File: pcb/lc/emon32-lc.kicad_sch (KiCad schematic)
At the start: 38 parts, among them J3 Conn_02x05_Odd_Even, J4 RJ12, J5 Conn_Coaxial, J6 USB_C_Receptacle_USB2.0, J7 Conn_01x03_Male, J8 Conn_02x04_Odd_Even, J9 Conn_01x03_Male, SW1 SW_Push, U2 AT24CS01-STUM, U3 ATSAMD11D14A-M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

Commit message: * [PCB LC]
  - Change to MCP1501 reference
  - Some retouching of traces
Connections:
- net UART_DBG_RX: now also J7.1 (Pin_1); no longer J7.2 (Pin_2)
- net UART_DBG_TX: now also J7.2 (Pin_2); no longer J7.1 (Pin_1)
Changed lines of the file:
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@@
     (effects (font (size 1.27 1.27)) (justify right bottom))
   )
-  (label "UART_DBG_RX" (at 139.7 91.44 0)
+  (label "UART_DBG_RX" (at 139.7 88.9 0)
     (effects (font (size 1.27 1.27)) (justify left bottom))
   )
@@
     (effects (font (size 1.27 1.27)) (justify right bottom))
   )
-  (label "UART_DBG_TX" (at 139.7 88.9 0)
+  (label "UART_DBG_TX" (at 139.7 91.44 0)
     (effects (font (size 1.27 1.27)) (justify left bottom))
   )
@@
       (reference "SW1") (unit 1) (value "SW_Push") (footprint "Button_Switch_SMD:SW_Push_1P1T_NO_CK_KMR2")
     )
+    (path "/00000000-0000-0000-0000-00005f9d8558/9b0fd944-1be1-4119-ab33-3408a03db8f9"
+      (reference "U1") (unit 1) (value "MCP1501-10xCH") (footprint "Package_TO_SOT_SMD:SOT-23-6")
+    )
     (path "/1b288fd6-808c-45f9-a4e3-2cd86772c113"
       (reference "U2") (unit 1) (value "AT24CS01-STUM") (footprint "Package_TO_SOT_SMD:SOT-23-5")
@@
       (reference "U4") (unit 5) (value "MCP6004") (footprint "Package_SO:TSSOP-14_4.4x5mm_P0.65mm")
     )
-    (path "/00000000-0000-0000-0000-00005f9d8558/00000000-0000-0000-0000-0000601e02e9"
-      (reference "U5") (unit 1) (value "REF3012") (footprint "Package_TO_SOT_SMD:SOT-23")
-    )
     (path "/40c84522-bb6c-4723-8d08-8ecfeeb4840b"

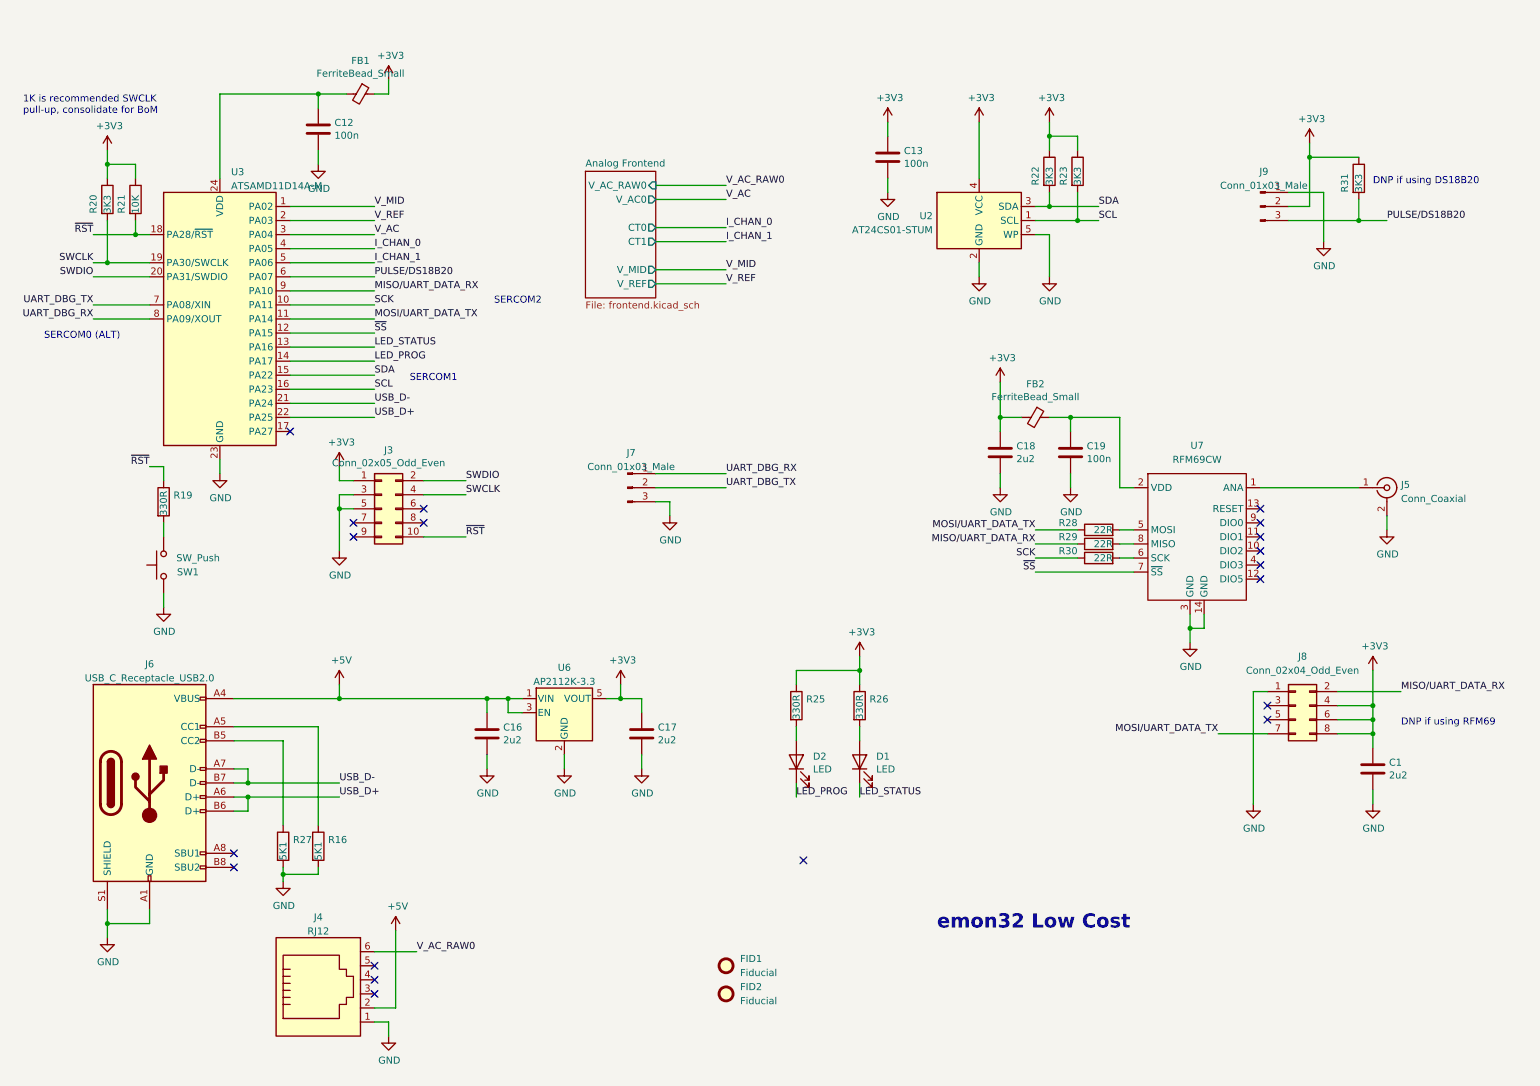
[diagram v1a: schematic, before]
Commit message: * [PCB LC]
  - Revise USB routing/spacing
  - Remove CT current out burden resistors
  - Add AAF filter, revise ADC input filter values
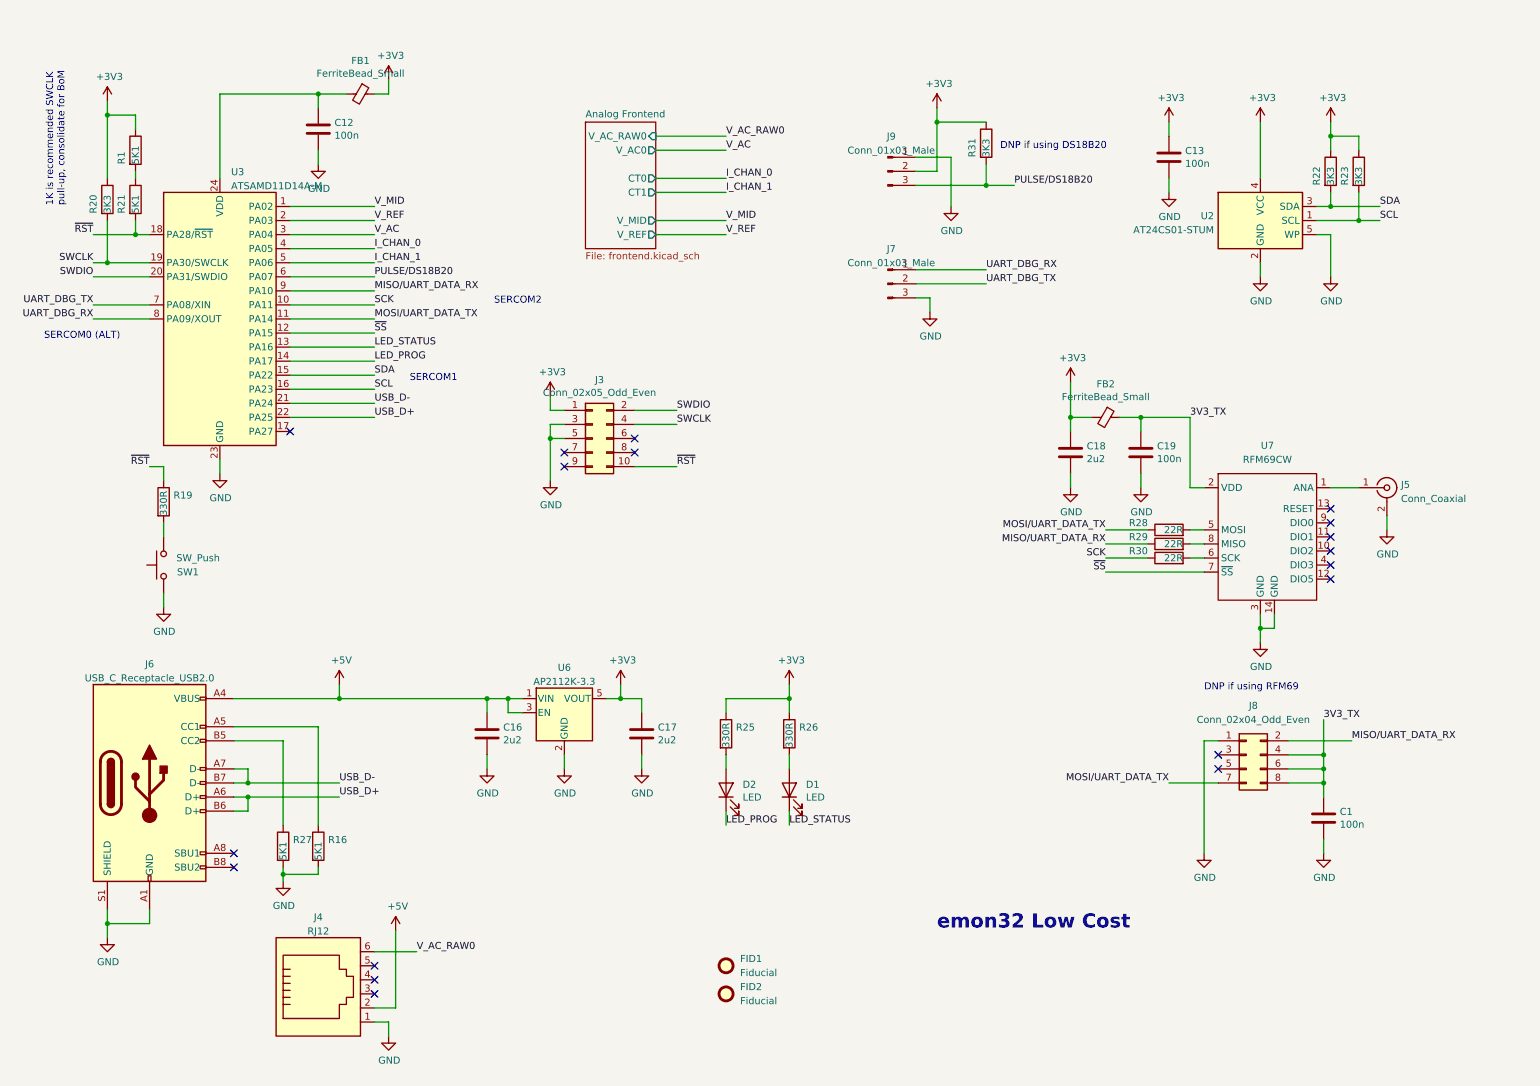
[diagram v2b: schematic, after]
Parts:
- added R1: 5K1, Resistor_SMD:R_0402_1005Metric, symbol Device:R
- C1: value 2u2 -> 100n; footprint Capacitor_SMD:C_0603_1608Metric_Pad1.08x0.95mm_HandSolder -> Capacitor_SMD:C_0402_1005Metric
- R21: value 10K -> 5K1
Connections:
- net +3V3: now also R1.1; no longer C1.1, J8.4 (Pin_4), J8.6 (Pin_6), J8.8 (Pin_8), R21.1
- net 3V3_TX: now reaches C19.1, FB2.1, U7.2 (VDD)
- net 3V3_TX: now also C1.1, J8.4 (Pin_4), J8.6 (Pin_6), J8.8 (Pin_8)
- new net: R1.2, R21.1
- no-connect marks 19 -> 18
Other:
- moved on the sheet: C13, C18, C19, D1, D2, FB2, J3, J7, J8, J9, R22, R23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

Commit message: * [PCB LC]
  - Bump to KiCad 7
  - Recalculate ADC input RC filter
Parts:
- C16, C17: value 2u2 -> 10u

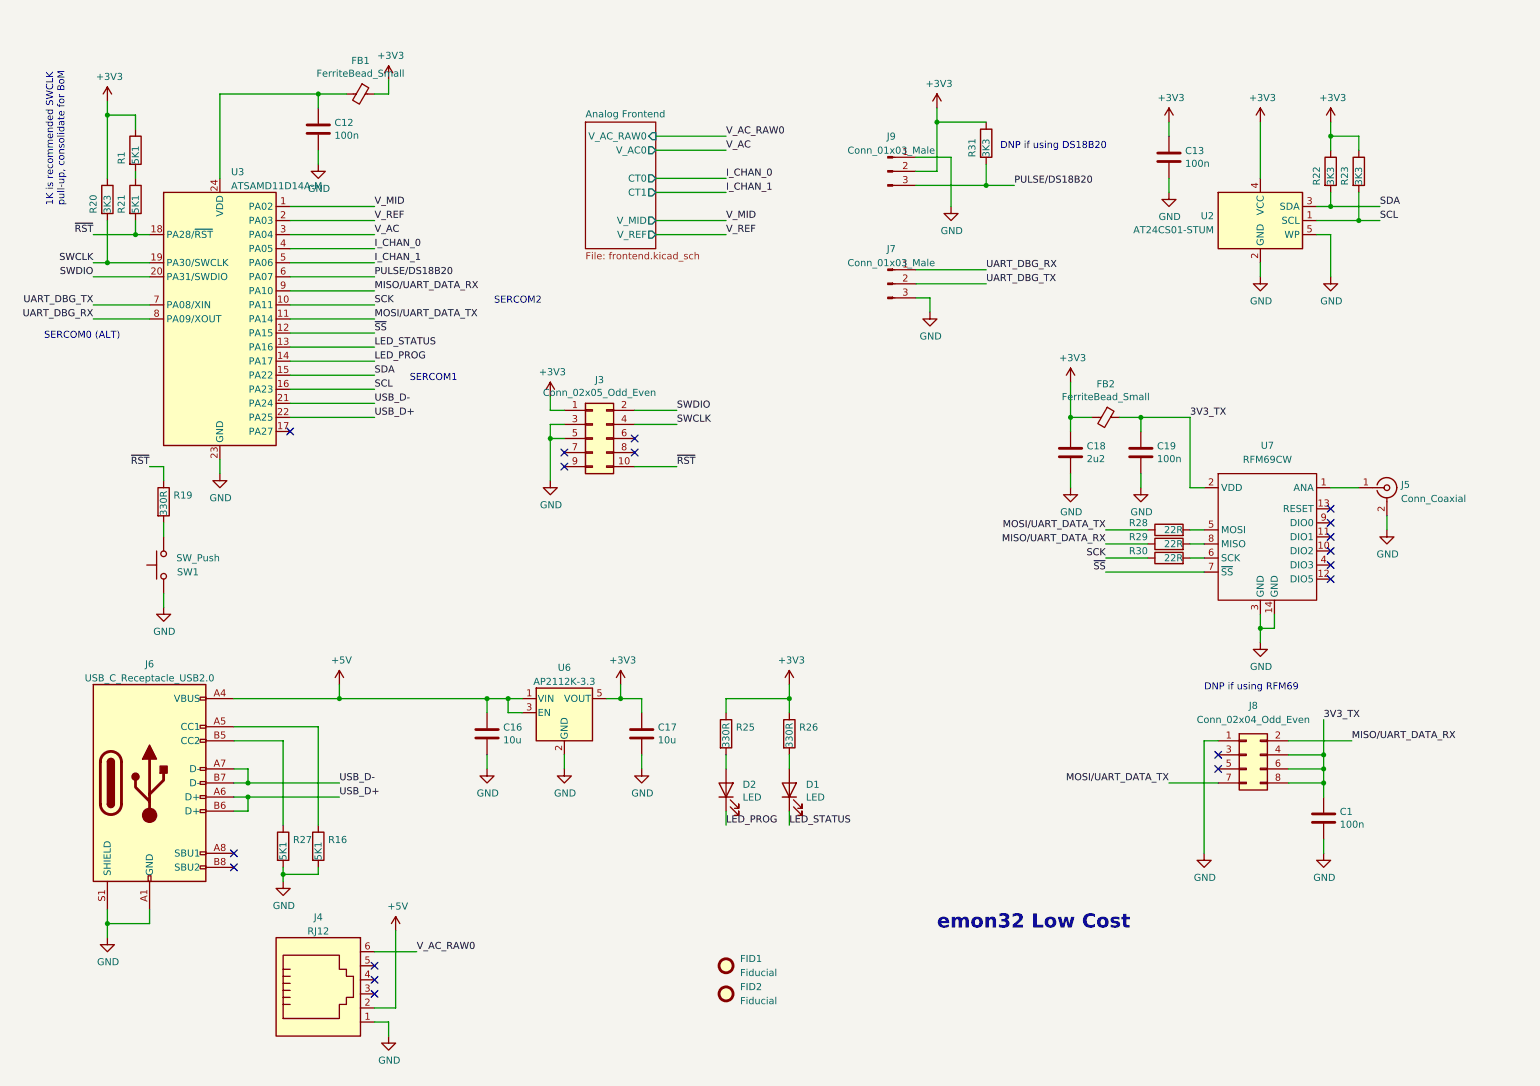
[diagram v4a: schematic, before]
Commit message: * [PCB LC]
  - First iteration of changes from LC-0.1dev -> LC-0.1
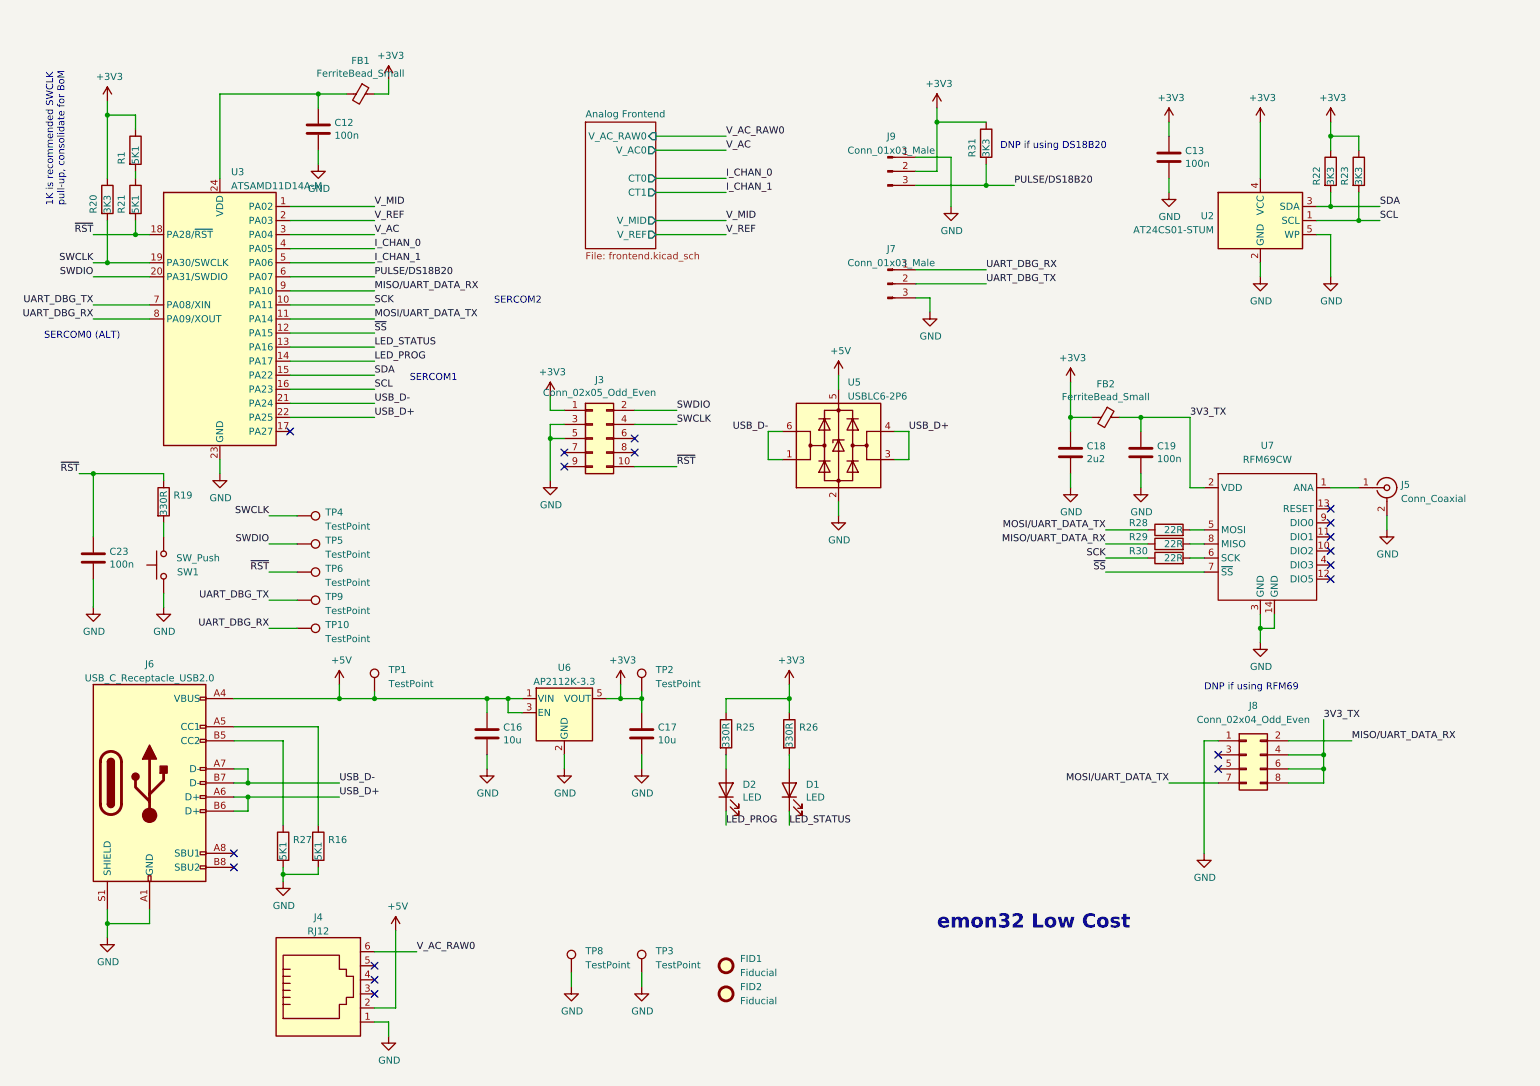
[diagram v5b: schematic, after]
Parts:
- removed C1: 100n, Capacitor_SMD:C_0402_1005Metric, symbol Device:C
- added C23: 100n, Capacitor_SMD:C_0402_1005Metric, symbol Device:C
- added TP1, TP10, TP2, TP3, TP4, TP5, TP6, TP8, TP9: TestPoint, TestPoint:TestPoint_Pad_D1.5mm, symbol Connector:TestPoint
- added U5: USBLC6-2P6, Package_TO_SOT_SMD:SOT-666, symbol Power_Protection:USBLC6-2P6
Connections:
- net +3V3: now also TP2.1
- net +5V: now also TP1.1, U5.5 (VBUS)
- net GND: now also C23.2, TP3.1, TP8.1, U5.2 (GND)
- net SWCLK: now also TP4.1
- net SWDIO: now also TP5.1
- net UART_DBG_RX: now also TP10.1
- net UART_DBG_TX: now also TP9.1
- net USB_D+: now also U5.3 (I/O2), U5.4 (I/O2)
- net USB_D-: now also U5.1 (I/O1), U5.6 (I/O1)
- net ~{RST}: now also C23.1, TP6.1
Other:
- company: (none) -> Tilt Ltd
- title: (none) -> emon32 Low Cost
